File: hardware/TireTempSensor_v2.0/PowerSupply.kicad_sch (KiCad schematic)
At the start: 9 parts

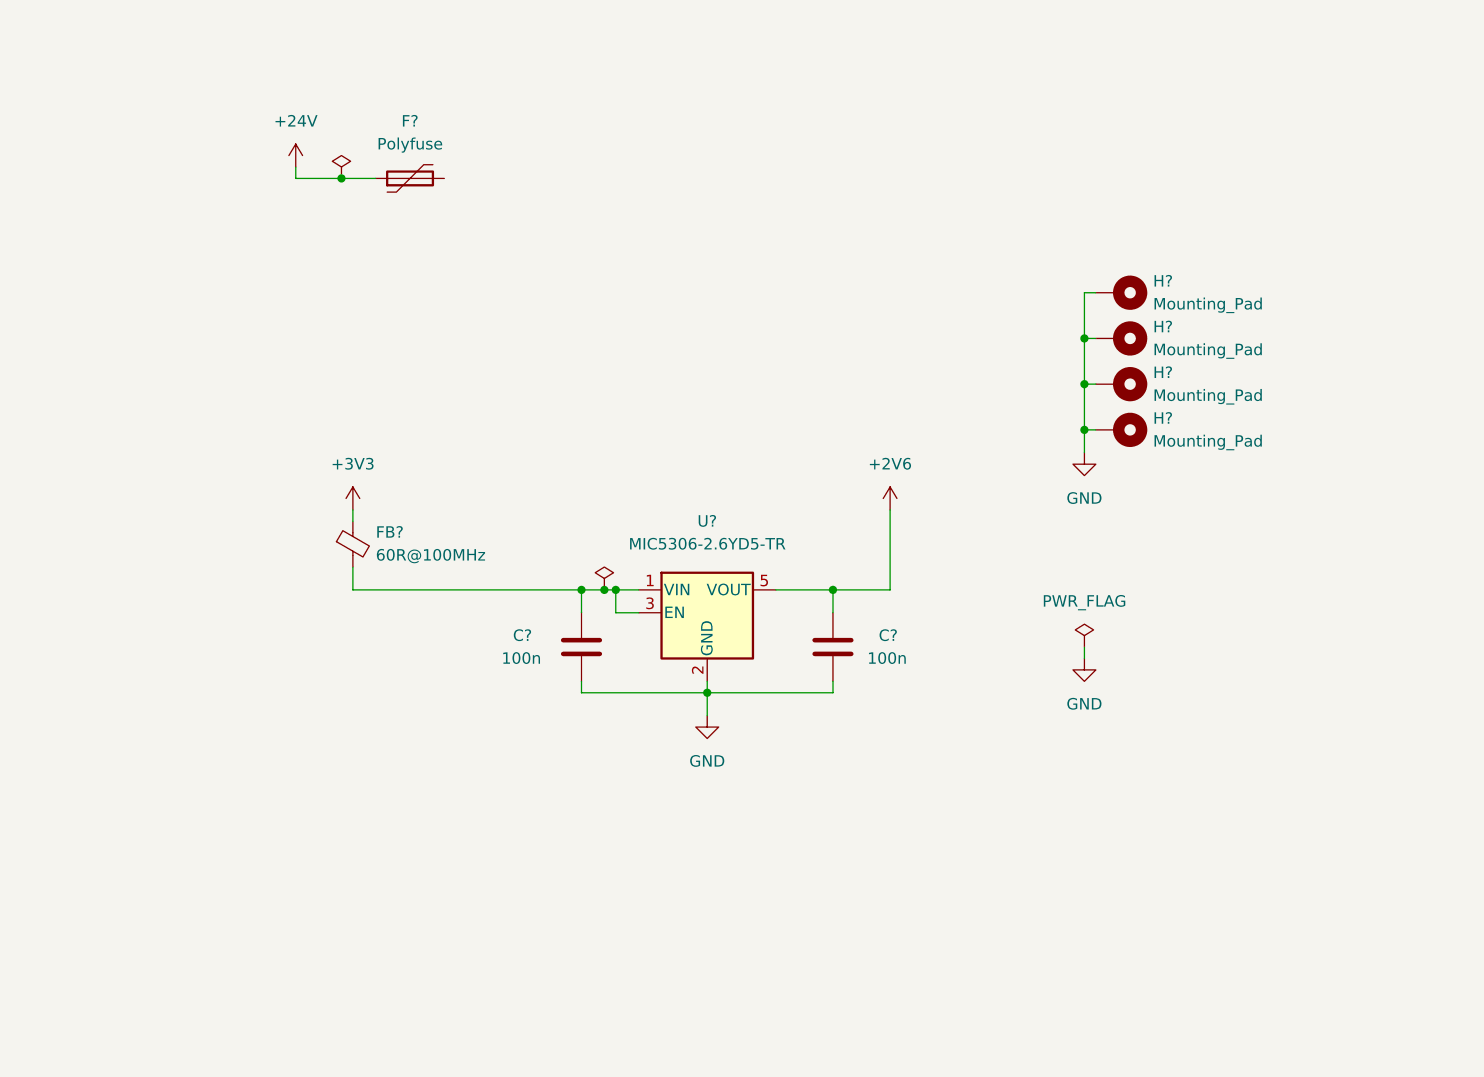
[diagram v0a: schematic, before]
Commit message: PFET & buck caps models
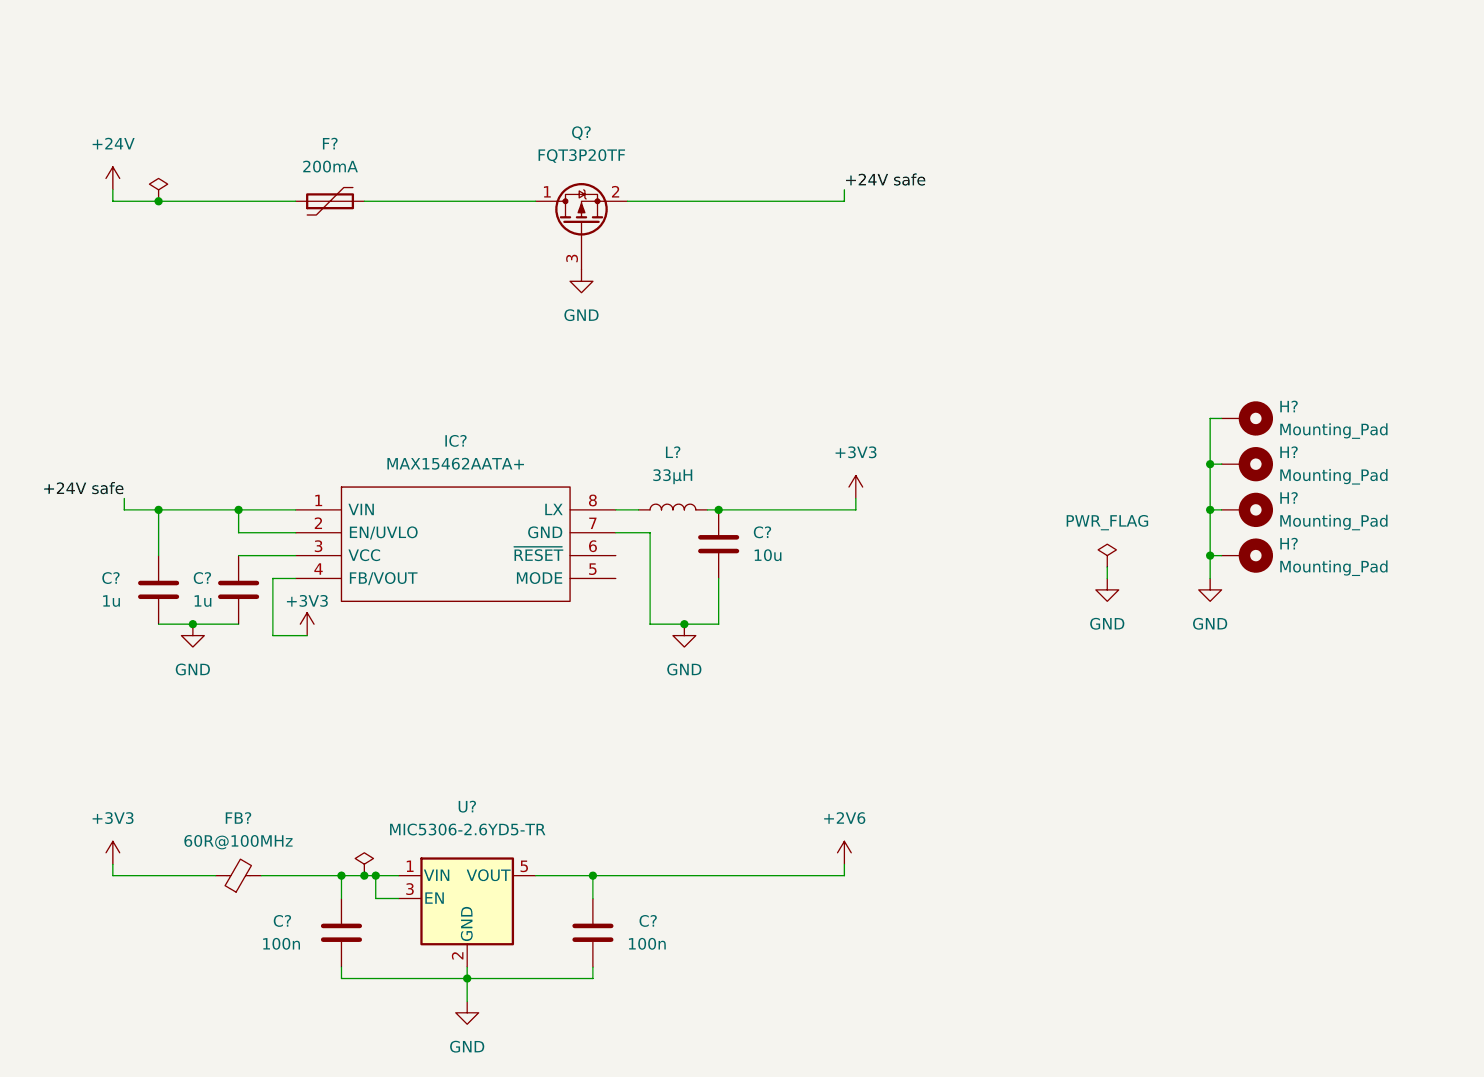
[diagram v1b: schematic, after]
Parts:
- removed FB?: 60R@100MHz, Inductor_SMD:L_0603_1608Metric, symbol Device:FerriteBead_Small
- added C? (x2): 1u, Capacitor_SMD:C_0603_1608Metric, symbol Device:C
- added C?: 10u, Capacitor_SMD:C_0603_1608Metric, symbol Device:C
- added FB?: 60R@100MHz, Inductor_SMD:L_0603_1608Metric, symbol Device:FerriteBead_Small
- added IC?: MAX15462AATA+, SON50P300X200X80-8N, symbol buck:MAX15462AATA+
- added L?: 33μH, symbol Device:L
- added Q?: FQT3P20TF, symbol Device:Q_PMOS_DSG
- F?: value Polyfuse -> 200mA
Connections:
- net +3V3: now also C?.1, FB?.1, IC?.4 (FB/VOUT), L?.2
- net GND: now also C?.2, C?.2, C?.2, IC?.7 (GND), Q?.3 (G)
- net at C?.1, U?.1 (VIN), U?.3 (EN): now also FB?.2
- net at F?.2: now also Q?.1 (D)
- new net: C?.1, IC?.3 (VCC)
- new net: IC?.8 (LX), L?.1
- new net +24V safe: C?.1, IC?.1 (VIN), IC?.2 (EN/UVLO), Q?.2 (S)
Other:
- title: (none) -> Power supply
- moved on the sheet: C?, F?, H?, U?

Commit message: erc tests passed
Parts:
- gave numbers to parts that had none: 15
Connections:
- no-connect marks 0 -> 2
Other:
- moved on the sheet: C12, C13, C14, C15, C16, F1, FB2, H1, H2, H3, H4, IC1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

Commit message: footprints added
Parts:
- C16: footprint Capacitor_SMD:C_0603_1608Metric -> Capacitor_SMD:C_1206_3216Metric
- F1: footprint Fuse:Fuse_0805_2012Metric -> Capacitor_SMD:C_1206_3216Metric
- IC1: footprint SON50P300X200X80-8N -> BuckSyncLib:SON50P300X200X80-8N
- L1: footprint (none) -> Inductor_SMD:L_Vishay_IFSC-1515AH_4x4x1.8mm
- Q1: footprint (none) -> Mosfet:SOT-223-4-NFET

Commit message: rough pcb layout
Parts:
- U2: footprint TSOT23-5:TSOT-23-5 -> Package_TO_SOT_SMD:SOT-23-5
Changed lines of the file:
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@@
     (property "Reference" "U2" (id 0) (at 124.46 132.08 0))
     (property "Value" "MIC5306-2.6YD5-TR" (id 1) (at 124.46 134.62 0))
-    (property "Footprint" "TSOT23-5:TSOT-23-5" (id 2) (at 124.46 133.985 0)
+    (property "Footprint" "Package_TO_SOT_SMD:SOT-23-5" (id 2) (at 124.46 133.985 0)
       (effects (font (size 1.27 1.27)) hide)
     )

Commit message: some pcb connections
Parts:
- added JP1: SolderJumper_2_Open, Jumper:SolderJumper-2_P1.3mm_Open_TrianglePad1.0x1.5mm, symbol Jumper:SolderJumper_2_Open
- F1: footprint Capacitor_SMD:C_1206_3216Metric -> Fuse:Fuse_1210_3225Metric
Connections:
- net +24V safe: now also JP1.2 (B)
- net at F1.2, Q1.1 (D): now also JP1.1 (A)
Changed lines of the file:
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@@
   (junction (at 90.17 99.06) (diameter 0) (color 0 0 0 0)
+  )
+  (junction (at 147.32 64.77) (diameter 0) (color 0 0 0 0)
+  )
+  (junction (at 127 64.77) (diameter 0) (color 0 0 0 0)
   )
   (junction (at 90.17 64.77) (diameter 0) (color 0 0 0 0)
@@
     (stroke (width 0) (type default) (color 0 0 0 0))
   )
+  (wire (pts (xy 147.32 52.07) (xy 147.32 64.77))
+    (stroke (width 0) (type default) (color 0 0 0 0))
+  )
   (wire (pts (xy 86.36 99.06) (xy 90.17 99.06))
     (stroke (width 0) (type default) (color 0 0 0 0))
@@
     (stroke (width 0) (type default) (color 0 0 0 0))
   )
+  (wire (pts (xy 140.97 52.07) (xy 147.32 52.07))
+    (stroke (width 0) (type default) (color 0 0 0 0))
+  )
+  (wire (pts (xy 127 64.77) (xy 132.08 64.77))
+    (stroke (width 0) (type default) (color 0 0 0 0))
+  )
   (wire (pts (xy 99.06 104.14) (xy 105.41 104.14))
     (stroke (width 0) (type default) (color 0 0 0 0))
@@
     (stroke (width 0) (type default) (color 0 0 0 0))
   )
+  (wire (pts (xy 127 52.07) (xy 133.35 52.07))
+    (stroke (width 0) (type default) (color 0 0 0 0))
+  )
   (wire (pts (xy 167.64 97.79) (xy 167.64 99.06))
     (stroke (width 0) (type default) (color 0 0 0 0))
@@
     (stroke (width 0) (type default) (color 0 0 0 0))
   )
+  (wire (pts (xy 127 64.77) (xy 127 52.07))
+    (stroke (width 0) (type default) (color 0 0 0 0))
+  )
   (wire (pts (xy 110.49 149.86) (xy 110.49 151.13))
     (stroke (width 0) (type default) (color 0 0 0 0))
@@
     (stroke (width 0) (type default) (color 0 0 0 0))
   )
-  (wire (pts (xy 113.03 64.77) (xy 132.08 64.77))
+  (wire (pts (xy 113.03 64.77) (xy 127 64.77))
     (stroke (width 0) (type default) (color 0 0 0 0))
   )
@@
     (stroke (width 0) (type default) (color 0 0 0 0))
   )
+  (wire (pts (xy 147.32 64.77) (xy 166.37 64.77))
+    (stroke (width 0) (type default) (color 0 0 0 0))
+  )
   (wire (pts (xy 110.49 142.24) (xy 110.49 139.7))
     (stroke (width 0) (type default) (color 0 0 0 0))
@@
     (stroke (width 0) (type default) (color 0 0 0 0))
   )
-  (wire (pts (xy 142.24 64.77) (xy 166.37 64.77))
+  (wire (pts (xy 142.24 64.77) (xy 147.32 64.77))
     (stroke (width 0) (type default) (color 0 0 0 0))
   )
@@
     (pin "2")
   )
+  (symbol (lib_id "Jumper:SolderJumper_2_Open") (at 137.16 52.07 0) (unit 1)
+    (in_bom yes) (on_board yes) (fields_autoplaced)
+    (property "Reference" "JP1" (id 0) (at 137.16 45.72 0))
+    (property "Value" "SolderJumper_2_Open" (id 1) (at 137.16 48.26 0))
+    (property "Footprint" "Jumper:SolderJumper-2_P1.3mm_Open_TrianglePad1.0x1.5mm" (id 2) (at 137.16 52.07 0)
+      (effects (font (size 1.27 1.27)) hide)
+    )
+    (property "Datasheet" "~" (id 3) (at 137.16 52.07 0)
+      (effects (font (size 1.27 1.27)) hide)
+    )
+    (pin "1")
+    (pin "2")
+  )
   (symbol (lib_id "power:GND") (at 207.01 106.68 0) (mirror y) (unit 1)
     (in_bom yes) (on_board yes) (fields_autoplaced)
@@
     (property "Reference" "F1" (id 0) (at 109.22 58.42 90))
     (property "Value" "200mA" (id 1) (at 109.22 60.96 90))
-    (property "Footprint" "Capacitor_SMD:C_1206_3216Metric" (id 2) (at 114.3 63.5 0)
-      (effects (font (size 1.27 1.27)) (justify left) hide)
-    )
-    (property "Datasheet" "~" (id 3) (at 109.22 64.77 0)
-      (effects (font (size 1.27 1.27)) hide)
-    )
+    (property "Footprint" "Fuse:Fuse_1210_3225Metric" (id 2) (at 114.3 63.5 0)
+      (effects (font (size 1.27 1.27)) (justify left) hide)
+    )
+    (property "Datasheet" "https://www.mouser.pl/ProductDetail/Littelfuse/1210L020WR?qs=PWhpLWeW8wcFhN6lPv0ohQ%3D%3D" (id 3) (at 109.22 64.77 0)
+      (effects (font (size 1.27 1.27)) hide)
+    )

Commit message: footprint has been changed + some minor silkscreen changes
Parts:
- IC1: footprint BuckSyncLib:SON50P300X200X80-8N -> Package_DFN_QFN:TDFN-8-1EP_2x2mm_P0.5mm_EP0.8x1.2mm
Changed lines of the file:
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@@
     (property "Reference" "IC1" (id 0) (at 123.19 91.44 0))
     (property "Value" "MAX15462AATA+" (id 1) (at 123.19 93.98 0))
-    (property "Footprint" "BuckSyncLib:SON50P300X200X80-8N" (id 2) (at 137.16 96.52 0)
+    (property "Footprint" "Package_DFN_QFN:TDFN-8-1EP_2x2mm_P0.5mm_EP0.8x1.2mm" (id 2) (at 137.16 96.52 0)
       (effects (font (size 1.27 1.27)) (justify left) hide)
     )
-    (property "Datasheet" "https://pdfserv.maximintegrated.com/package_dwgs/21-0487.PDF" (id 3) (at 137.16 99.06 0)
+    (property "Datasheet" "" (id 3) (at 137.16 99.06 0)
       (effects (font (size 1.27 1.27)) (justify left) hide)
     )
